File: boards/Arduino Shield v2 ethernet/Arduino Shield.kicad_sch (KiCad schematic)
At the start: 11 parts, among them U1 A000062, U2 W5500

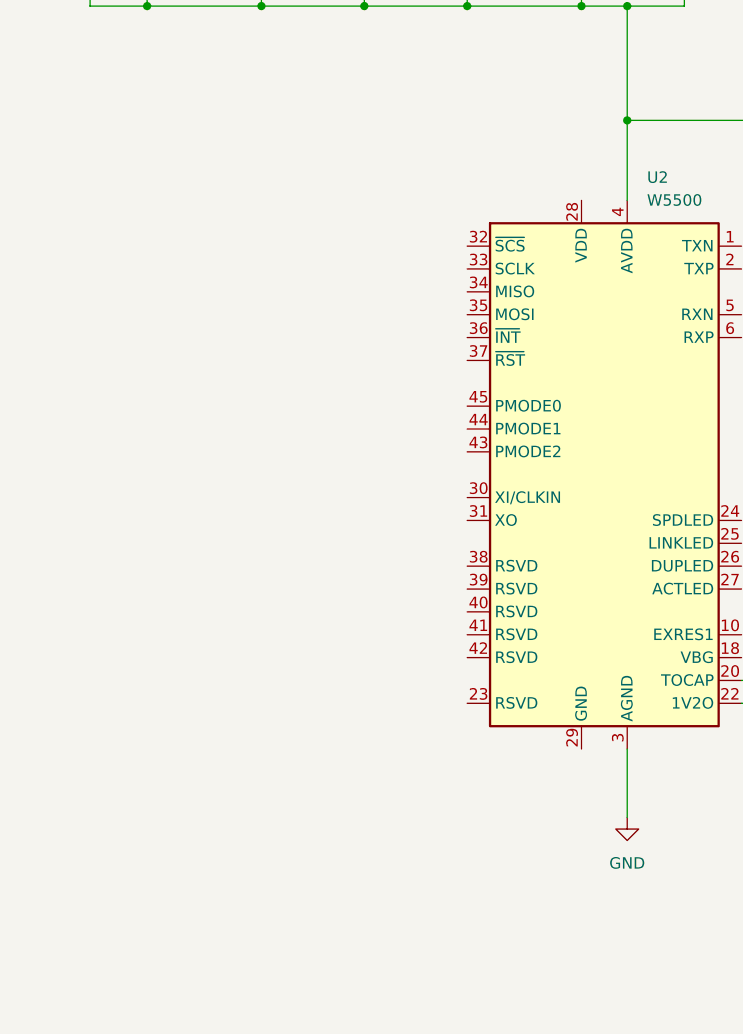
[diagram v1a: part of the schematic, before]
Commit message: Updated Ethernet Sheild
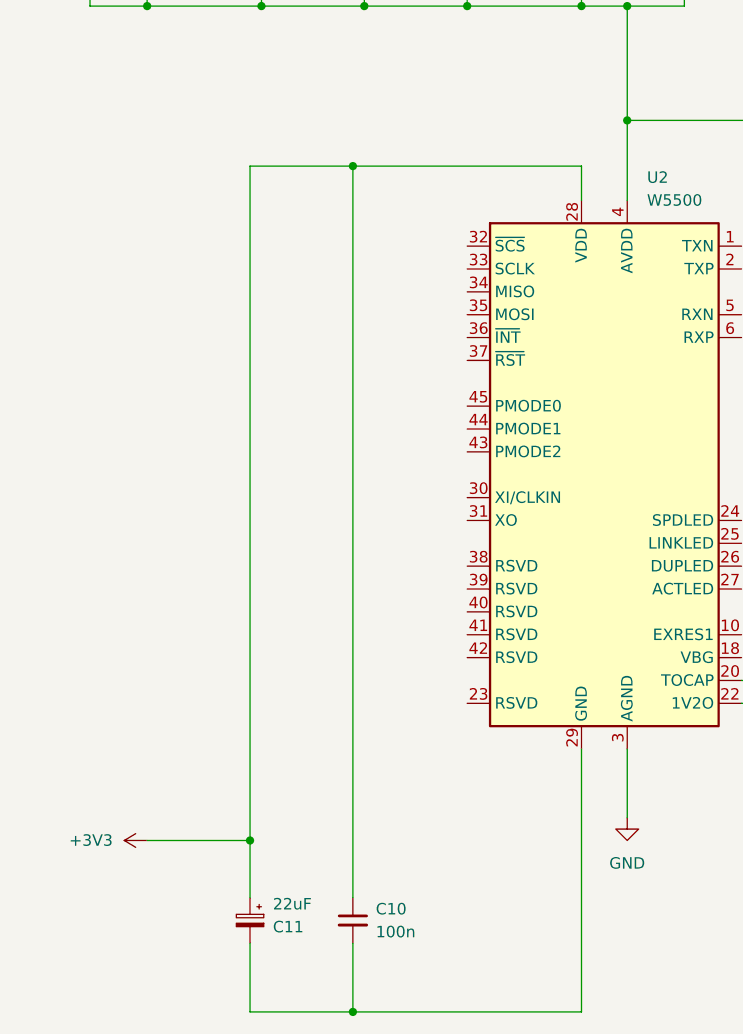
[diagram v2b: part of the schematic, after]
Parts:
- added C10: 100n, symbol Device:C_Small
- added C11: 22uF, symbol Device:C_Polarized_Small
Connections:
- net +3V3: now also U2.28 (VDD), C10.1, C11.1
- net at U2.29 (GND): now also C10.2, C11.2
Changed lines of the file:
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@@
   (junction (at 69.85 33.02) (diameter 0) (color 0 0 0 0)
   )
+  (junction (at 62.23 154.94) (diameter 0) (color 0 0 0 0)
+  )
   (junction (at 87.63 43.18) (diameter 0) (color 0 0 0 0)
   )
   (junction (at 92.71 55.88) (diameter 0) (color 0 0 0 0)
   )
+  (junction (at 62.23 60.96) (diameter 0) (color 0 0 0 0)
+  )
   (junction (at 63.5 43.18) (diameter 0) (color 0 0 0 0)
   )
@@
   (junction (at 39.37 43.18) (diameter 0) (color 0 0 0 0)
   )
+  (junction (at 50.8 135.89) (diameter 0) (color 0 0 0 0)
+  )
   (wire (pts (xy 99.06 43.18) (xy 99.06 40.64))
     (stroke (width 0) (type default))
   )
+  (wire (pts (xy 39.37 135.89) (xy 50.8 135.89))
+    (stroke (width 0) (type default))
+  )
   (wire (pts (xy 52.07 33.02) (xy 63.5 33.02))
     (stroke (width 0) (type default))
@@
     (stroke (width 0) (type default))
   )
+  (wire (pts (xy 87.63 125.73) (xy 87.63 154.94))
+    (stroke (width 0) (type default))
+  )
+  (wire (pts (xy 62.23 142.24) (xy 62.23 60.96))
+    (stroke (width 0) (type default))
+  )
   (wire (pts (xy 87.63 40.64) (xy 87.63 43.18))
     (stroke (width 0) (type default))
@@
     (stroke (width 0) (type default))
   )
+  (wire (pts (xy 50.8 135.89) (xy 50.8 60.96))
+    (stroke (width 0) (type default))
+  )
+  (wire (pts (xy 87.63 60.96) (xy 87.63 64.77))
+    (stroke (width 0) (type default))
+  )
   (wire (pts (xy 87.63 43.18) (xy 92.71 43.18))
     (stroke (width 0) (type default))
@@
     (stroke (width 0) (type default))
   )
+  (wire (pts (xy 62.23 154.94) (xy 62.23 147.32))
+    (stroke (width 0) (type default))
+  )
   (wire (pts (xy 63.5 43.18) (xy 74.93 43.18))
     (stroke (width 0) (type default))
   )
+  (wire (pts (xy 50.8 60.96) (xy 62.23 60.96))
+    (stroke (width 0) (type default))
+  )
   (wire (pts (xy 33.02 40.64) (xy 33.02 43.18))
     (stroke (width 0) (type default))
@@
     (stroke (width 0) (type default))
   )
+  (wire (pts (xy 50.8 154.94) (xy 62.23 154.94))
+    (stroke (width 0) (type default))
+  )
   (wire (pts (xy 92.71 55.88) (xy 92.71 64.77))
     (stroke (width 0) (type default))
   )
+  (wire (pts (xy 87.63 154.94) (xy 62.23 154.94))
+    (stroke (width 0) (type default))
+  )
   (wire (pts (xy 105.41 120.65) (xy 116.84 120.65))
     (stroke (width 0) (type default))
@@
     (stroke (width 0) (type default))
   )
+  (wire (pts (xy 62.23 60.96) (xy 87.63 60.96))
+    (stroke (width 0) (type default))
+  )
+  (wire (pts (xy 50.8 147.32) (xy 50.8 154.94))
+    (stroke (width 0) (type default))
+  )
   (wire (pts (xy 63.5 40.64) (xy 63.5 43.18))
     (stroke (width 0) (type default))
@@
     (stroke (width 0) (type default))
   )
+  (wire (pts (xy 50.8 142.24) (xy 50.8 135.89))
+    (stroke (width 0) (type default))
+  )
   (wire (pts (xy 39.37 33.02) (xy 52.07 33.02))
     (stroke (width 0) (type default))
@@
   (wire (pts (xy 115.57 116.84) (xy 116.84 116.84))
     (stroke (width 0) (type default))
+  )
+  (symbol (lib_id "power:+3V3") (at 39.37 135.89 90) (unit 1)
+    (in_bom yes) (on_board yes) (dnp no) (fields_autoplaced)
+    (property "Reference" "#PWR06" (at 43.18 135.89 0)
+      (effects (font (size 1.27 1.27)) hide)
+    )
+    (property "Value" "+3V3" (at 35.56 135.89 90)
+      (effects (font (size 1.27 1.27)) (justify left))
+    )
+    (property "Footprint" "" (at 39.37 135.89 0)
+      (effects (font (size 1.27 1.27)) hide)
+    )
+    (property "Datasheet" "" (at 39.37 135.89 0)
+      (effects (font (size 1.27 1.27)) hide)
+    )
+    (pin "1")
+    (instances
+      (project "Arduino Shield"
+        (path "/d32bdb2e-fa3a-461a-9e34-c0053c91b5d5"
+          (reference "#PWR06") (unit 1)
+        )
+      )
+    )
+  )
+  (symbol (lib_id "Device:C_Small") (at 62.23 144.78 0) (unit 1)
+    (in_bom yes) (on_board yes) (dnp no) (fields_autoplaced)
+    (property "Reference" "C10" (at 64.77 143.5163 0)
+      (effects (font (size 1.27 1.27)) (justify left))
+    )
+    (property "Value" "100n" (at 64.77 146.0563 0)
+      (effects (font (size 1.27 1.27)) (justify left))
+    )
+    (property "Footprint" "" (at 62.23 144.78 0)
+      (effects (font (size 1.27 1.27)) hide)
+    )
+    (property "Datasheet" "~" (at 62.23 144.78 0)
+      (effects (font (size 1.27 1.27)) hide)
+    )
+    (pin "1")
+    (pin "2")
+    (instances
+      (project "Arduino Shield"
+        (path "/d32bdb2e-fa3a-461a-9e34-c0053c91b5d5"
+          (reference "C10") (unit 1)
+        )
+      )
+    )
   )
   (symbol (lib_id "Interface_Ethernet:W5500") (at 90.17 95.25 0) (unit 1)
@@
         )
       )
+    )
+  )
+  (symbol (lib_id "Device:C_Polarized_Small") (at 50.8 144.78 0) (mirror y) (unit 1)
+    (in_bom yes) (on_board yes) (dnp no)
+    (property "Reference" "C11" (at 53.34 145.5039 0)
+      (effects (font (size 1.27 1.27)) (justify right))
+    )
+    (property "Value" "22uF" (at 53.34 142.9639 0)
+      (effects (font (size 1.27 1.27)) (justify right))
+    )
+    (property "Footprint" "" (at 50.8 144.78 0)
+      (effects (font (size 1.27 1.27)) hide)
+    )
+    (property "Datasheet" "~" (at 50.8 144.78 0)
+      (effects (font (size 1.27 1.27)) hide)
+    )
+    (pin "1")
+    (pin "2")
+    (instances
+      (project "Arduino Shield"
+        (path "/d32bdb2e-fa3a-461a-9e34-c0053c91b5d5"
+          (reference "C11") (unit 1)
+        )
+      )
